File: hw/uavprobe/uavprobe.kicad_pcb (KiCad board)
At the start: 2 copper layers, 0 parts

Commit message: Components import and model setup
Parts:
- added C1: 100n, Capacitor_SMD:C_0402_1005Metric, F.Cu at (163.5, 68.1)
- added C10: 1u, Capacitor_SMD:C_0402_1005Metric, F.Cu at (166.4, 76.0)
- added C11: 100n, Capacitor_SMD:C_0402_1005Metric, F.Cu at (169.2, 68.1)
- added C12: 100n, Capacitor_SMD:C_0402_1005Metric, F.Cu at (169.2, 70.0)
- added C13: 100n, Capacitor_SMD:C_0402_1005Metric, F.Cu at (169.2, 72.0)
- added C14: 100n, Capacitor_SMD:C_0402_1005Metric, F.Cu at (169.2, 74.0)
- added C15: 100n, Capacitor_SMD:C_0402_1005Metric, F.Cu at (169.2, 76.0)
- added C16: 100n, Capacitor_SMD:C_0402_1005Metric, F.Cu at (172.1, 68.1)
- added C17: 100n, Capacitor_SMD:C_0402_1005Metric, F.Cu at (172.1, 70.0)
- added C18: 100n, Capacitor_SMD:C_0402_1005Metric, F.Cu at (172.1, 72.0)
- added C19: 100p, Capacitor_SMD:C_0402_1005Metric, F.Cu at (172.1, 74.0)
- added C2: 10u, Capacitor_SMD:C_0402_1005Metric, F.Cu at (163.5, 70.0)
- added C20: 100p, Capacitor_SMD:C_0402_1005Metric, F.Cu at (172.1, 76.0)
- added C21: 10u, Capacitor_SMD:C_0402_1005Metric, F.Cu at (160.2, 105.1)
- added C22: 1u, Capacitor_SMD:C_0402_1005Metric, F.Cu at (160.2, 107.1)
- added C23: 10u, Capacitor_SMD:C_0402_1005Metric, F.Cu at (160.2, 109.0)
- added C24: 100n, Capacitor_SMD:C_0402_1005Metric, F.Cu at (160.2, 111.0)
- added C25: 100n, Capacitor_SMD:C_0402_1005Metric, F.Cu at (160.2, 113.0)
- added C26: 100n, Capacitor_SMD:C_0402_1005Metric, F.Cu at (160.2, 114.9)
- added C27: 12p, Capacitor_SMD:C_0402_1005Metric, F.Cu at (160.2, 116.9)
- added C28: 12p, Capacitor_SMD:C_0402_1005Metric, F.Cu at (160.2, 118.9)
- added C29: 1u, Capacitor_SMD:C_0402_1005Metric, F.Cu at (140.9, 61.8)
- added C3: 27p, Capacitor_SMD:C_0402_1005Metric, F.Cu at (163.5, 72.0)
- added C30: 1u, Capacitor_SMD:C_0402_1005Metric, F.Cu at (140.9, 63.8)
- added C31: 1u, Capacitor_SMD:C_0402_1005Metric, F.Cu at (140.9, 65.8)
- added C32: 1u, Capacitor_SMD:C_0402_1005Metric, F.Cu at (140.9, 67.7)
- added C33: 1u, Capacitor_SMD:C_0402_1005Metric, F.Cu at (143.7, 61.8)
- added C34: 1u, Capacitor_SMD:C_0402_1005Metric, F.Cu at (143.7, 63.8)
- added C35: 1u, Capacitor_SMD:C_0402_1005Metric, F.Cu at (143.7, 65.8)
- added C36: 1u, Capacitor_SMD:C_0402_1005Metric, F.Cu at (143.7, 67.7)
- added C37: 1u, Capacitor_SMD:C_0402_1005Metric, F.Cu at (146.6, 61.8)
- added C38: 10u, Capacitor_SMD:C_0402_1005Metric, F.Cu at (146.6, 63.8)
- added C39: 1u, Capacitor_SMD:C_0402_1005Metric, F.Cu at (146.6, 65.8)
- added C4: 27p, Capacitor_SMD:C_0402_1005Metric, F.Cu at (163.5, 74.0)
- added C40: 1u, Capacitor_SMD:C_0402_1005Metric, F.Cu at (146.6, 67.7)
- added C5: 100n, Capacitor_SMD:C_0402_1005Metric, F.Cu at (163.5, 76.0)
- added C6: 10u, Capacitor_SMD:C_0402_1005Metric, F.Cu at (166.4, 68.1)
- added C7: 100n, Capacitor_SMD:C_0402_1005Metric, F.Cu at (166.4, 70.0)
- added C8: 1u, Capacitor_SMD:C_0402_1005Metric, F.Cu at (166.4, 72.0)
- added C9: 100n, Capacitor_SMD:C_0402_1005Metric, F.Cu at (166.4, 74.0)
- added D1: NUP2105L, Package_TO_SOT_SMD:SOT-23, F.Cu at (176.0, 69.5)
- added D2: NUP2105L, Package_TO_SOT_SMD:SOT-23, F.Cu at (176.0, 74.1)
- added D3: RP2040 fault, LED_SMD:LED_0402_1005Metric, F.Cu at (155.3, 109.0)
- added D4: USB peripheral fault, LED_SMD:LED_0402_1005Metric, F.Cu at (155.3, 111.0)
- added D5: High-Speed, LED_SMD:LED_0402_1005Metric, F.Cu at (155.3, 113.0)
- added D6: Suspend, LED_SMD:LED_0402_1005Metric, F.Cu at (155.3, 115.0)
- added D7: USB host power, LED_SMD:LED_0402_1005Metric, F.Cu at (155.3, 117.0)
- added D8: RP2040 power, LED_SMD:LED_0402_1005Metric, F.Cu at (155.3, 119.0)
- added D9: USB peripheral power, LED_SMD:LED_0402_1005Metric, F.Cu at (155.3, 121.0)
- added FL1: ECLAMP8052P.TCT, Import:ECLAMP8052PTCT, F.Cu at (174.0, 106.8)
- added IC1: UCLAMP3306P.TCT, Import:SON50P160X160X65-7N, F.Cu at (155.6, 82.2)
- added J1: USB_C_Receptacle_USB2.0_14P, Connector_USB:USB_C_Receptacle_GCT_USB4105-xx-A_16P_TopMnt_Horizontal, F.Cu at (164.6, 99.4)
- added J10: SERIAL1 (flow control), Connector_JST:JST_GH_BM06B-GHS-TBT_1x06-1MP_P1.25mm_Vertical, F.Cu at (111.9, 95.3)
- added J11: SERIAL1 (GPS/I2C), Connector_JST:JST_GH_BM06B-GHS-TBT_1x06-1MP_P1.25mm_Vertical, F.Cu at (111.9, 102.9)
- added J12: SERIAL1 (Lidar), Connector_JST:JST_GH_BM04B-GHS-TBT_1x04-1MP_P1.25mm_Vertical, F.Cu at (123.7, 95.3)
- added J13: I^{2}C (Lidar), Connector_JST:JST_GH_BM04B-GHS-TBT_1x04-1MP_P1.25mm_Vertical, F.Cu at (134.2, 64.7)
- added J14: I^{2}C, Connector_JST:JST_GH_BM04B-GHS-TBT_1x04-1MP_P1.25mm_Vertical, F.Cu at (134.2, 72.3)
- added J15: USB2, Connector_JST:JST_GH_BM04B-GHS-TBT_1x04-1MP_P1.25mm_Vertical, F.Cu at (134.2, 80.0)
- added J16: CAN1, Connector_JST:JST_GH_BM04B-GHS-TBT_1x04-1MP_P1.25mm_Vertical, F.Cu at (134.2, 87.6)
- added J17: CAN2, Connector_JST:JST_GH_BM04B-GHS-TBT_1x04-1MP_P1.25mm_Vertical, F.Cu at (134.2, 95.3)
- added J2: 6-pin A, Connector_JST:JST_GH_BM06B-GHS-TBT_1x06-1MP_P1.25mm_Vertical, F.Cu at (111.9, 64.7)
- added J3: 4-pin A, Connector_JST:JST_GH_BM04B-GHS-TBT_1x04-1MP_P1.25mm_Vertical, F.Cu at (123.7, 64.7)
- added J4: SERIAL1, Connector_JST:JST_GH_BM04B-GHS-TBT_1x04-1MP_P1.25mm_Vertical, F.Cu at (123.7, 72.3)
- added J5: SERIAL2, Connector_JST:JST_GH_BM04B-GHS-TBT_1x04-1MP_P1.25mm_Vertical, F.Cu at (123.7, 80.0)
- added J6: SERIAL1/2, Connector_JST:JST_GH_BM06B-GHS-TBT_1x06-1MP_P1.25mm_Vertical, F.Cu at (111.9, 72.3)
- added J7: SERIAL2/1, Connector_JST:JST_GH_BM06B-GHS-TBT_1x06-1MP_P1.25mm_Vertical, F.Cu at (111.9, 80.0)
- added J8: 6-pin B, Connector_JST:JST_GH_BM06B-GHS-TBT_1x06-1MP_P1.25mm_Vertical, F.Cu at (111.9, 87.6)
- added J9: 4-pin B, Connector_JST:JST_GH_BM04B-GHS-TBT_1x04-1MP_P1.25mm_Vertical, F.Cu at (123.7, 87.6)
- added R10: 61.9k, Resistor_SMD:R_0402_1005Metric, F.Cu at (151.5, 95.1)
- added R11: 5.1k, Resistor_SMD:R_0402_1005Metric, F.Cu at (151.5, 97.1)
- added R12: 5.1k, Resistor_SMD:R_0402_1005Metric, F.Cu at (151.5, 99.1)
- added R13: 5.1k, Resistor_SMD:R_0402_1005Metric, F.Cu at (151.5, 101.1)
- added R14: 5.1k, Resistor_SMD:R_0402_1005Metric, F.Cu at (151.5, 103.1)
- added R15: 5.1k, Resistor_SMD:R_0402_1005Metric, F.Cu at (151.5, 105.1)
- added R16: 10k, Resistor_SMD:R_0402_1005Metric, F.Cu at (151.5, 107.0)
- added R17: 1M, Resistor_SMD:R_0402_1005Metric, F.Cu at (154.4, 95.1)
- added R18: 12k, Resistor_SMD:R_0402_1005Metric, F.Cu at (154.4, 97.1)
- added R19: 51k, Resistor_SMD:R_0402_1005Metric, F.Cu at (154.4, 99.1)
- added R2: 10k, Resistor_SMD:R_0402_1005Metric, F.Cu at (171.7, 61.8)
- added R20: 150R, Resistor_SMD:R_0402_1005Metric, F.Cu at (154.4, 101.1)
- added R21: 150R, Resistor_SMD:R_0402_1005Metric, F.Cu at (154.4, 103.1)
- added R22: 10R, Resistor_SMD:R_0402_1005Metric, F.Cu at (154.4, 105.1)
- added R23: 51k, Resistor_SMD:R_0402_1005Metric, F.Cu at (154.4, 107.0)
- added R24: 10R, Resistor_SMD:R_0402_1005Metric, F.Cu at (157.3, 95.1)
- added R25: 51k, Resistor_SMD:R_0402_1005Metric, F.Cu at (157.3, 97.1)
- added R26: 95R, Resistor_SMD:R_0402_1005Metric, F.Cu at (157.3, 99.1)
- added R27: 150R, Resistor_SMD:R_0402_1005Metric, F.Cu at (157.3, 101.1)
- added R28: 95R, Resistor_SMD:R_0402_1005Metric, F.Cu at (157.3, 103.1)
- added R29: 1k, Resistor_SMD:R_0402_1005Metric, F.Cu at (177.5, 65.8)
- added R3: 27, Resistor_SMD:R_0402_1005Metric, F.Cu at (171.7, 63.8)
- added R4: 27, Resistor_SMD:R_0402_1005Metric, F.Cu at (171.7, 65.8)
- added R5: 1k, Resistor_SMD:R_0402_1005Metric, F.Cu at (174.6, 61.8)
- added R6: 60, Resistor_SMD:R_0402_1005Metric, F.Cu at (174.6, 63.8)
- added R7: 60, Resistor_SMD:R_0402_1005Metric, F.Cu at (174.6, 65.8)
- added R8: 60, Resistor_SMD:R_0402_1005Metric, F.Cu at (177.5, 61.8)
- added R9: 60, Resistor_SMD:R_0402_1005Metric, F.Cu at (177.5, 63.8)
- added SW1: Boot, Button_Switch_SMD:SW_SPST_B3U-1000P, F.Cu at (175.3, 88.4)
- added SW2: Reset, Button_Switch_SMD:SW_SPST_B3U-1000P, F.Cu at (173.4, 101.6)
- added TP1: SWCLK, TestPoint:TestPoint_Pad_D1.5mm, F.Cu at (151.8, 62.6)
- added TP2: SWD, TestPoint:TestPoint_Pad_D1.5mm, F.Cu at (151.8, 66.2)
- added TP3: GND, TestPoint:TestPoint_Pad_D1.5mm, F.Cu at (151.8, 69.7)
- added TP4: 1.1 V, TestPoint:TestPoint_Pad_D1.5mm, F.Cu at (151.8, 73.3)
- added TP5: 3.3 V, TestPoint:TestPoint_Pad_D1.5mm, F.Cu at (151.8, 76.8)
- added TP6: 3.3 V (HUB), TestPoint:TestPoint_Pad_D1.5mm, F.Cu at (151.8, 109.8)
- added TP7: USB host power, TestPoint:TestPoint_Pad_D1.5mm, F.Cu at (151.8, 113.4)
- added TP8: RP2040 power, TestPoint:TestPoint_Pad_D1.5mm, F.Cu at (151.8, 116.9)
- added TP9: USB peripheral power, TestPoint:TestPoint_Pad_D1.5mm, F.Cu at (151.8, 120.5)
- added U1: W25Q16JVSS, Package_SO:SOIC-8_5.3x5.3mm_P1.27mm, F.Cu at (167.2, 80.4)
- added U2: NCP1117-5.0_SOT223, Package_TO_SOT_SMD:SOT-223-3_TabPin2, F.Cu at (167.0, 88.0)
- added U3: RP2040, Package_DFN_QFN:QFN-56-1EP_7x7mm_P0.4mm_EP3.2x3.2mm, F.Cu at (177.1, 81.6)
- added U4: TJA1051T-3, Package_SO:SOIC-8_3.9x4.9mm_P1.27mm, F.Cu at (157.8, 70.5)
- added U5: TJA1051T-3, Package_SO:SOIC-8_3.9x4.9mm_P1.27mm, F.Cu at (157.8, 77.0)
- added U6: NCP1117-5.0_SOT223, Package_TO_SOT_SMD:SOT-223-3_TabPin2, F.Cu at (166.6, 108.3)
- added U7: TPS2561, Package_SON:VSON-10-1EP_3x3mm_P0.5mm_EP1.65x2.4mm_ThermalVias, F.Cu at (173.1, 96.8)
- added U8: USB2412-DZK, Import:QFN50P500X500X100-29N, F.Cu at (165.6, 116.1)
- added Y1: ABLS-12.000MHZ-B4-T, Import:XTAL_ABLS-12.000MHZ-B4-T, F.Cu at (161.9, 64.0)
- added Y2: 24MHz, Crystal:Crystal_SMD_Abracon_ABM3B-4Pin_5.0x3.2mm, F.Cu at (173.0, 115.0)

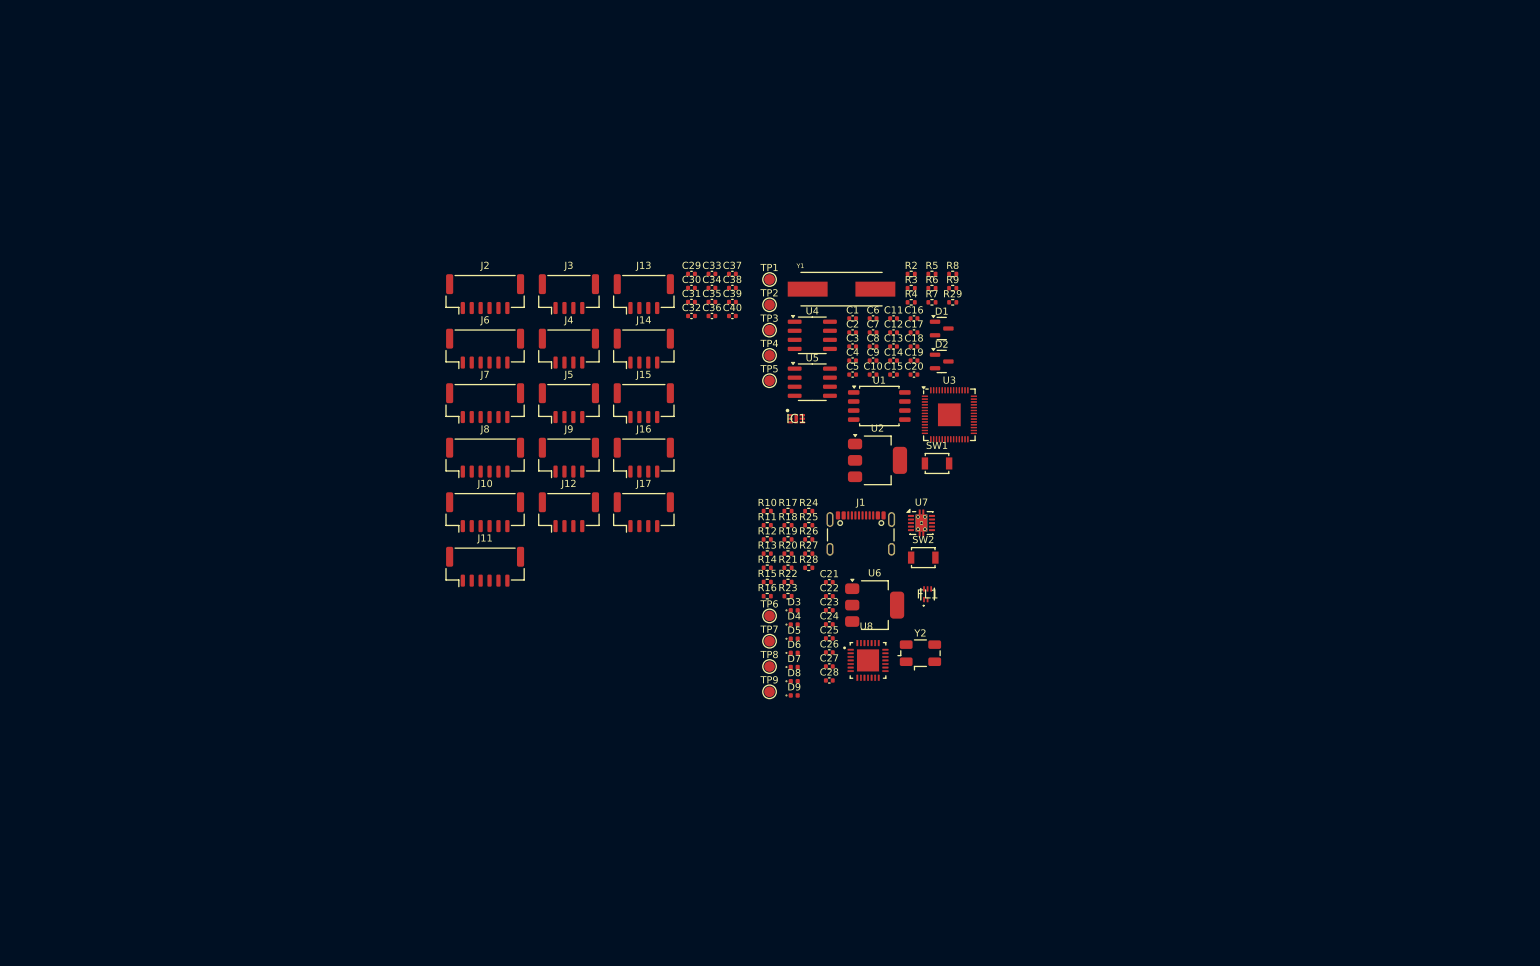
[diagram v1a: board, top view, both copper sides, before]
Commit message: Design rules and net classes
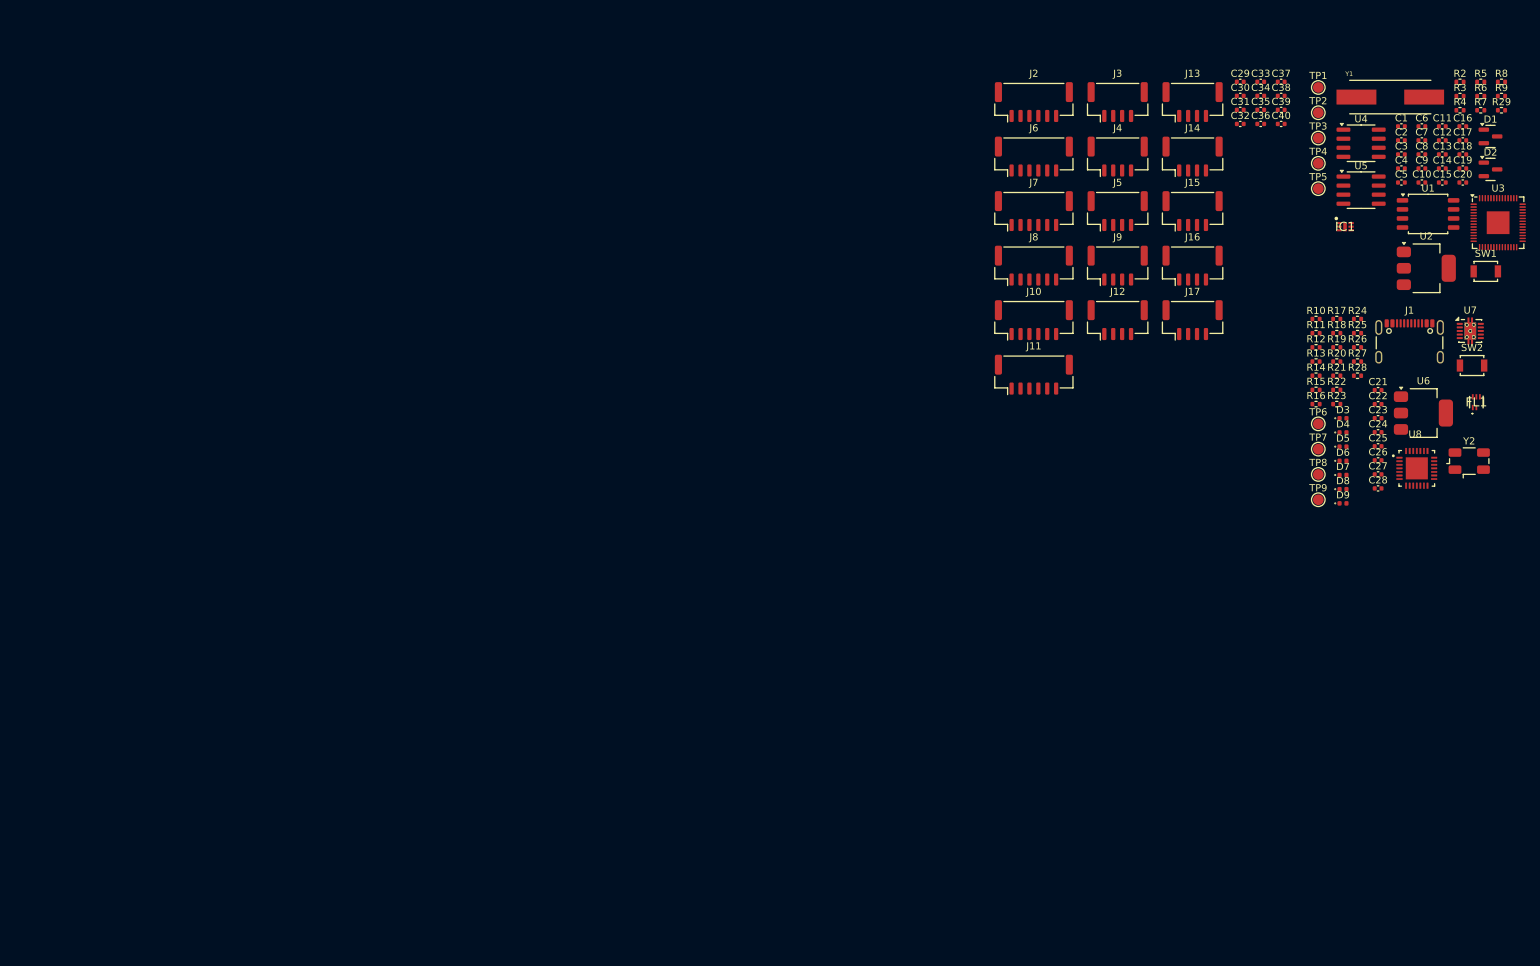
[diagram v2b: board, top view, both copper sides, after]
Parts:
- moved J12 81.6 mm to (200.7, 68.3)
- moved J3 81.6 mm to (200.7, 37.7)
- moved J4 81.6 mm to (200.7, 45.4)
- moved J5 81.6 mm to (200.7, 53.0)
- moved J9 81.6 mm to (200.7, 60.7)
- moved C1 81.6 mm to (240.5, 41.1)
- moved C10 81.6 mm to (243.4, 49.0)
- moved C11 81.6 mm to (246.2, 41.1)
- moved C12 81.6 mm to (246.2, 43.1)
- moved C13 81.6 mm to (246.2, 45.1)
- moved C14 81.6 mm to (246.2, 47.0)
- moved C15 81.6 mm to (246.2, 49.0)
- moved C16 81.6 mm to (249.1, 41.1)
- moved C17 81.6 mm to (249.1, 43.1)
- moved C18 81.6 mm to (249.1, 45.1)
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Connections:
- net Net-(FL1-I/O+_IN) renamed /USB/USB2_HUB_D+
- net Net-(FL1-I/O-_IN) renamed /USB/USB2_HUB_D-
- net Net-(U8-USBDM_UP) renamed /USB/USBC_D-
- net Net-(U8-USBDP_UP) renamed /USB/USBC_D+

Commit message: Training layout
Lessons were learned, let's restart.
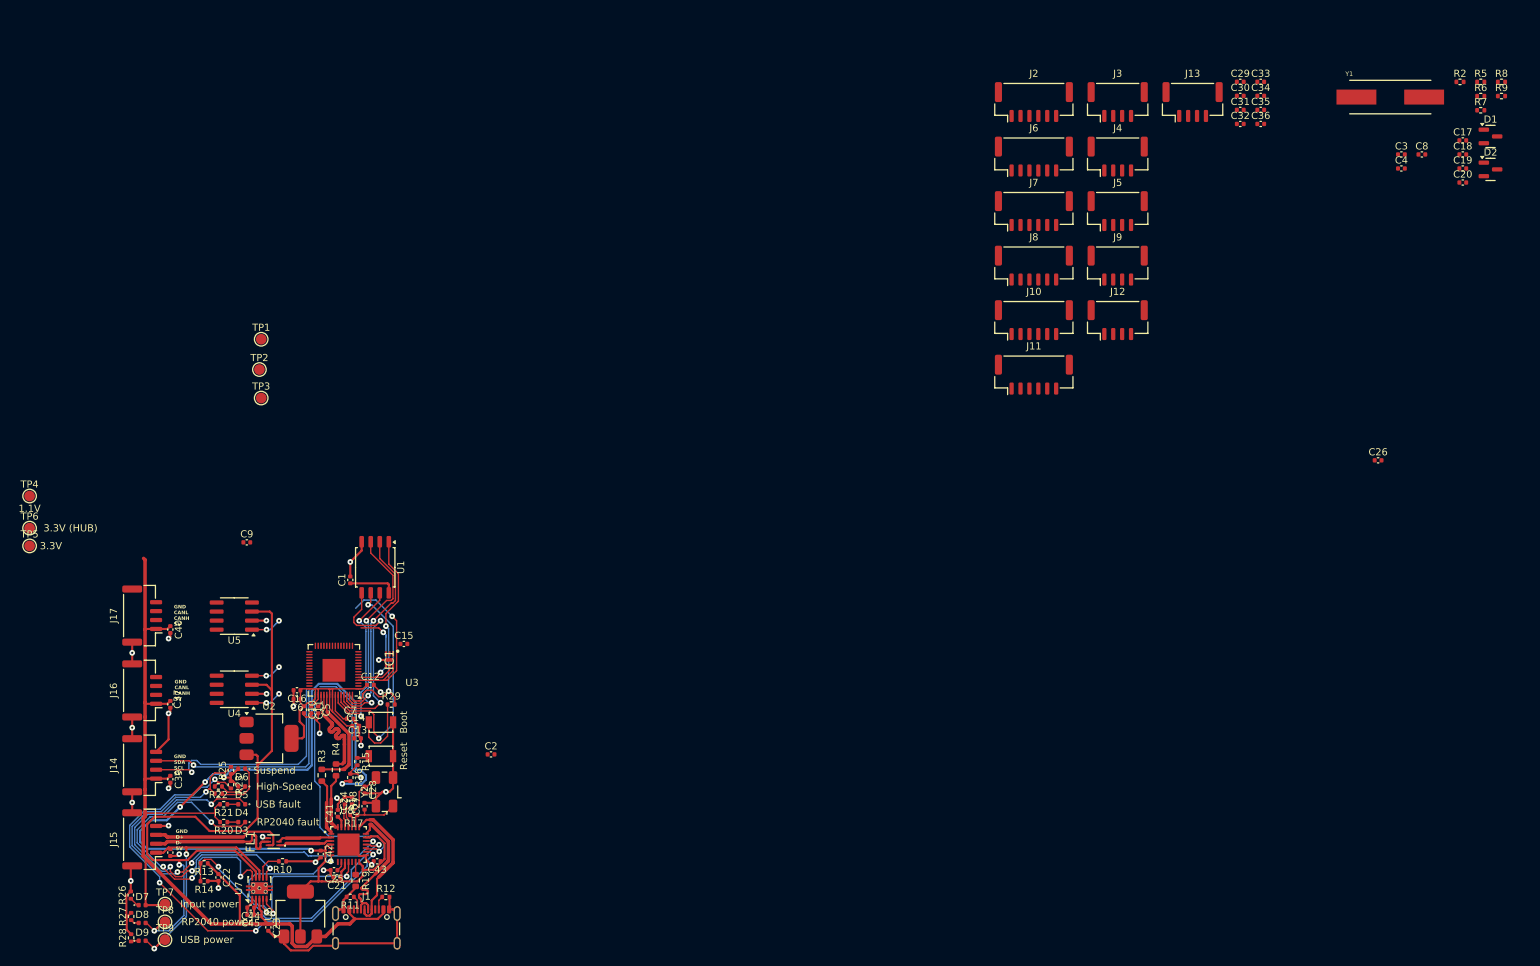
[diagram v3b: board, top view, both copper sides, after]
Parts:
- added C41: 5u, Capacitor_SMD:C_0402_1005Metric, F.Cu at (91.2, 137.5)
- added C42: 5u, Capacitor_SMD:C_0402_1005Metric, F.Cu at (88.8, 143.2)
- added C43: 5u, Capacitor_SMD:C_0402_1005Metric, F.Cu at (96.8, 144.2)
- added C44: 10u, Capacitor_SMD:C_0402_1005Metric, F.Cu at (79.0, 150.8)
- added C45: 10u, Capacitor_SMD:C_0402_1005Metric, F.Cu at (79.0, 151.8)
- C21: value 10u -> 5u
- D4: value USB peripheral fault -> USB fault
- D7: value USB host power -> Input power
- D9: value USB peripheral power -> USB power
- R19, R3, R4: footprint Resistor_SMD:R_0402_1005Metric -> Resistor_SMD:R_0603_1608Metric
- TP4: value 1.1 V -> 1.1V
- TP5: value 3.3 V -> 3.3V
- TP6: value 3.3 V (HUB) -> 3.3V (HUB)
- moved R28 189.3 mm to (62.2, 155.0), turned to 90 degrees
- moved R27 188.9 mm to (62.2, 152.0), turned to 90 degrees
- moved C38 188.6 mm to (67.8, 143.0), turned to -90 degrees
- moved R26 188.5 mm to (62.2, 149.0), turned to 90 degrees
- moved TP5 187.6 mm to (48.0, 100.0)
- moved U7 187.0 mm to (80.2, 148.0), turned to 90 degrees
- moved TP4 186.8 mm to (48.0, 93.0)
- moved R3 186.0 mm to (89.0, 132.2), turned to 90 degrees
- moved R4 182.9 mm to (91.0, 131.4), turned to 90 degrees
- moved C39 182.0 mm to (67.8, 132.7), turned to -90 degrees
- moved C16 181.7 mm to (85.5, 120.2), turned to 180 degrees
- moved TP6 181.4 mm to (48.0, 97.5)
- moved FL1 179.7 mm to (82.2, 141.5), turned to 90 degrees
- moved D9 179.3 mm to (63.8, 155.4)
- moved D8 179.1 mm to (63.8, 152.9)
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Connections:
- net Net-(U3-USB_DM) renamed /RP2040/USBRPI_D-
- net Net-(U3-USB_DP) renamed /RP2040/USBRPI_D+
- R29 pad 2: +3.3V -> Net-(U1-~{CS})
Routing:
- net /Connectors/VBUS: track 0.00 -> 138.4 mm
- net +3.3V (HUB): track 0.00 -> 133.4 mm, vias 0 -> 5
- net GND: track 0.00 -> 130.2 mm, vias 0 -> 24
- net /RP2040/VBUS1: track 0.00 -> 96.5 mm, vias 0 -> 2
- net Net-(U8-HS_IND): track 0.00 -> 67.1 mm, vias 0 -> 4
- net Net-(U8-SUSP_IND/NON_REM0): track 0.00 -> 60.9 mm, vias 0 -> 4
- net /Connectors/I2C_SDA: track 0.00 -> 55.3 mm, vias 0 -> 2
- net /USB/~{RESET}: track 0.00 -> 52.5 mm, vias 0 -> 2
- net /Connectors/I2C_SCL: track 0.00 -> 49.5 mm, vias 0 -> 3
- net /USB/FAULT2: track 0.00 -> 46.3 mm, vias 0 -> 4
- net /USB/FAULT1: track 0.00 -> 44.5 mm, vias 0 -> 4
- net +3.3V: track 0.00 -> 43.8 mm
- net Net-(U8-VBUS_DET): track 0.00 -> 38.5 mm, vias 0 -> 2
- net /Connectors/VBUS2: track 0.00 -> 36.9 mm, vias 0 -> 2
- net /RP2040/SCLK: track 0.00 -> 33.2 mm, vias 0 -> 2
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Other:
- board text added: "GND CANL CANH 5V"
- board text added: "GND D+ D- 5V"
- board text added: "GND SDA SCL 5V"

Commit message: Layout revision 1
Pre-DRC
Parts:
- added REF**: Symbol_Attention_Triangle_8x7mm_Copper, Symbol:Symbol_Attention_Triangle_8x7mm_Copper, F.Cu at (123.6, 75.7)
- D3: value RP2040 fault -> MCU fault
- D8: value RP2040 power -> MCU power
- J10: value SERIAL1 (flow control) -> SERIAL1 (flow)
- R19, R4: footprint Resistor_SMD:R_0603_1608Metric -> Resistor_SMD:R_0402_1005Metric
- TP6: value 3.3V (HUB) -> 3.3V HUB
- TP7: value USB host power -> 5V USB in
- TP8: value RP2040 power -> 5V USB1
- TP9: value USB peripheral power -> 5V USB2
- moved R5 137.4 mm to (130.2, 99.2), turned to -90 degrees
- moved C8 135.8 mm to (126.2, 113.8), turned to -90 degrees
- moved R2 135.5 mm to (131.2, 102.5), turned to -90 degrees
- moved D1 132.8 mm to (121.6, 61.9), turned to -90 degrees
- moved D2 131.5 mm to (121.5, 51.6), turned to 90 degrees
- moved C17 131.3 mm to (121.0, 72.0), turned to 180 degrees
- moved C18 130.7 mm to (118.4, 45.0), turned to 90 degrees
- moved R9 130.7 mm to (124.9, 53.5)
- moved R8 130.7 mm to (124.9, 51.5), turned to 180 degrees
- moved R7 128.8 mm to (124.9, 61.9)
- moved R6 128.8 mm to (124.9, 59.9), turned to 180 degrees
- moved C29 126.0 mm to (116.9, 110.2)
- moved C19 124.9 mm to (124.9, 60.9)
- moved C20 124.3 mm to (124.9, 52.5)
- moved TP8 122.3 mm to (127.2, 46.2)
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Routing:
- net GND: track 130.2 -> 419.1 mm, vias 24 -> 105
- net /Connectors/VBUS: track 138.4 -> 337.7 mm, vias 0 -> 3
- net /Connectors/UART1_TX: track 0.00 -> 161.5 mm, vias 0 -> 9
- net /Connectors/UART1_RX: track 0.00 -> 151.3 mm, vias 0 -> 7
- net Net-(U3-SWCLK): track 0.00 -> 103.7 mm, vias 0 -> 4
- net Net-(U3-SWD): track 0.00 -> 92.3 mm, vias 0 -> 4
- net /Connectors/UART2_TX: track 0.00 -> 88.1 mm, vias 0 -> 6
- net /Connectors/I2C_SCL: track 49.5 -> 137.5 mm, vias 3 -> 4
- net /RP2040/CAN2_SILENT: track 0.00 -> 80.7 mm, vias 0 -> 6
- net +3.3V: track 43.8 -> 123.9 mm, vias 0 -> 4
- net /Connectors/I2C_SDA: track 55.3 -> 134.6 mm, vias 2 -> 6
- net /RP2040/CAN2_RX: track 0.00 -> 78.9 mm, vias 0 -> 6
- net /RP2040/CAN2_TX: track 4.32 -> 81.9 mm, vias 2 -> 6
- net /Connectors/UART2_RX: track 0.00 -> 72.0 mm, vias 0 -> 3
- net /RP2040/CAN1_SILENT: track 0.00 -> 59.0 mm, vias 0 -> 4
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- added copper zone on B.Cu, net GND
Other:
- board outline added: 31 x 120 mm
- board text added: "5V CANH CANL GND"
- board text added: "GND RTS CTS RX TX 5V"
- board text added: "GND RX TX 5V"
- board text added: "GND RX2 TX2 RX1 TX1 5V"
- board text added: "GND SDA SCL RX TX 5V"
- board text added: "GND TX1 RX1 TX2 RX2 5V"
- board text added: "Ports with special pinout!"
- board text added: "SCL SDA 5V GND"
- board text added: "TX RX 5V GND"
- board text removed: "GND CANL CANH 5V"
